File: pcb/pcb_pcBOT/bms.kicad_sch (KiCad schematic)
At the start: 23 parts, among them J201 Lipo, U201 BQ25896RTW

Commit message: manual merge
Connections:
- net SCL_I2C is gone; now on net I2C_SCL: R203.2
- net SDA_I2C is gone; now on net I2C_SDA: R201.2
- net SYS_3.5-4.5V is gone; now on net SYS: C205.1, C207.1, JP202.1 (A), L201.2, U201.15 (SYS), U201.16 (SYS)
- net +5V: now also JP202.2 (B)
- net GND: now also C207.2
- net OTG_HOST: no longer R202.2
- net REGN: now also C204.2
- net STAT: now also R202.2
- net VBUS: now also JP201.1 (A), JP203.1 (A); no longer JP201.2 (B), U201.1 (VBUS)
- net SW: now reaches C203.1, L201.1, U201.19 (SW), U201.20 (SW)
- net BTST: now reaches C203.2, U201.21 (BTST)
- net BAT: now reaches C206.1, J201.1 (Pin_1), U201.13 (BAT), U201.14 (BAT)
- net TS: now reaches R207.2, R208.1, U201.11 (TS)
- net ILIM: now reaches R206.2, U201.10 (ILIM)
- net I2C_SCL: now reaches U201.5 (SCL)
- net PHY: no longer names the net of JP203.2 (B), U201.2 (PSEL)
- net VREF renamed +3.3V
- new net: JP201.2 (B), U201.1 (VBUS)
- no-connect marks 1 -> 0
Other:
- moved on the sheet: R206

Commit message: avancement des schematics
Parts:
- renumbered JP203 to JP202, JP202 to JP203
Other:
- company: ENSEA -> ENSEA G5
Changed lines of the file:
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@@
 		(title "Bms bq25896 (typical application)")
 		(rev "1.0")
-		(company "ENSEA")
+		(company "ENSEA G5")
 	)
 	(junction
@@
 		(dnp no)
 		(fields_autoplaced yes)
-		(property "Reference" "#PWR0204"
+		(property "Reference" "#PWR0206"
 			(at 107.95 77.47 0)
 			(effects
@@
 			(project "pcb_pcBOT"
 				(path "/704e4da3-8ee7-458f-8a0f-3fc97e8dc2a6/d67675e6-7dac-4bc7-9bdf-0364d005735e"
-					(reference "#PWR0204")
+					(reference "#PWR0206")
 					(unit 1)
 				)
@@
 		(on_board yes)
 		(dnp no)
-		(property "Reference" "JP203"
+		(property "Reference" "JP202"
 			(at 119.38 70.104 0)
 			(effects
@@
 			(project "pcb_pcBOT"
 				(path "/704e4da3-8ee7-458f-8a0f-3fc97e8dc2a6/d67675e6-7dac-4bc7-9bdf-0364d005735e"
-					(reference "JP203")
+					(reference "JP202")
 					(unit 1)
 				)
@@
 		(on_board yes)
 		(dnp no)
-		(property "Reference" "#PWR0203"
+		(property "Reference" "#PWR0204"
 			(at 74.93 67.31 0)
 			(effects
@@
 			(project "pcb_pcBOT"
 				(path "/704e4da3-8ee7-458f-8a0f-3fc97e8dc2a6/d67675e6-7dac-4bc7-9bdf-0364d005735e"
-					(reference "#PWR0203")
+					(reference "#PWR0204")
 					(unit 1)
 				)
@@
 		(dnp no)
 		(fields_autoplaced yes)
-		(property "Reference" "JP202"
+		(property "Reference" "JP203"
 			(at 189.23 57.15 0)
 			(effects
@@
 			(project "pcb_pcBOT"
 				(path "/704e4da3-8ee7-458f-8a0f-3fc97e8dc2a6/d67675e6-7dac-4bc7-9bdf-0364d005735e"
-					(reference "JP202")
+					(reference "JP203")
 					(unit 1)
 				)
@@
 		(dnp no)
 		(fields_autoplaced yes)
-		(property "Reference" "#PWR0210"
+		(property "Reference" "#PWR0211"
 			(at 182.88 74.93 0)
 			(effects
@@
 			(project "pcb_pcBOT"
 				(path "/704e4da3-8ee7-458f-8a0f-3fc97e8dc2a6/d67675e6-7dac-4bc7-9bdf-0364d005735e"
-					(reference "#PWR0210")
+					(reference "#PWR0211")
 					(unit 1)
 				)
@@
 		(dnp no)
 		(fields_autoplaced yes)
-		(property "Reference" "#PWR0212"
+		(property "Reference" "#PWR0203"
 			(at 69.85 99.06 0)
 			(effects
@@
 			(project ""
 				(path "/704e4da3-8ee7-458f-8a0f-3fc97e8dc2a6/d67675e6-7dac-4bc7-9bdf-0364d005735e"
-					(reference "#PWR0212")
+					(reference "#PWR0203")
 					(unit 1)
 				)
@@
 		(dnp no)
 		(fields_autoplaced yes)
-		(property "Reference" "#PWR0206"
+		(property "Reference" "#PWR0207"
 			(at 133.35 111.76 0)
 			(effects
@@
 			(project ""
 				(path "/704e4da3-8ee7-458f-8a0f-3fc97e8dc2a6/d67675e6-7dac-4bc7-9bdf-0364d005735e"
-					(reference "#PWR0206")
+					(reference "#PWR0207")
 					(unit 1)
 				)
@@
 		(dnp no)
 		(fields_autoplaced yes)
-		(property "Reference" "#PWR0207"
+		(property "Reference" "#PWR0210"
 			(at 170.18 74.93 0)
 			(effects
@@
 			(project "pcb_pcBOT"
 				(path "/704e4da3-8ee7-458f-8a0f-3fc97e8dc2a6/d67675e6-7dac-4bc7-9bdf-0364d005735e"
-					(reference "#PWR0207")
+					(reference "#PWR0210")
 					(unit 1)
 				)
@@
 		(dnp no)
 		(fields_autoplaced yes)
-		(property "Reference" "#PWR0211"
+		(property "Reference" "#PWR0212"
 			(at 187.96 101.6 0)
 			(effects
@@
 			(project "pcb_pcBOT"
 				(path "/704e4da3-8ee7-458f-8a0f-3fc97e8dc2a6/d67675e6-7dac-4bc7-9bdf-0364d005735e"
-					(reference "#PWR0211")
-					(unit 1)
-				)
+					(reference "#PWR0212")
+					(unit 1)
+				)

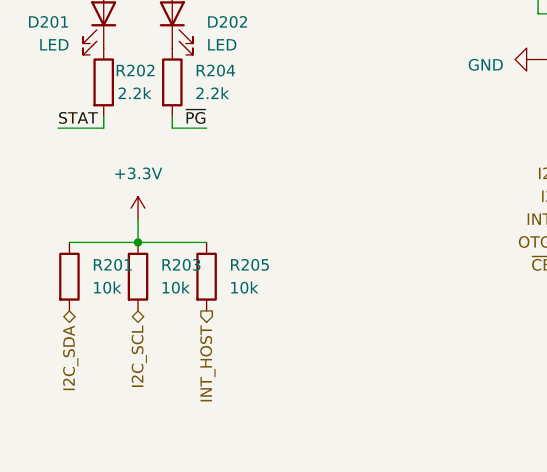
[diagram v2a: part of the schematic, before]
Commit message: ajout du module nrf + petites corrections
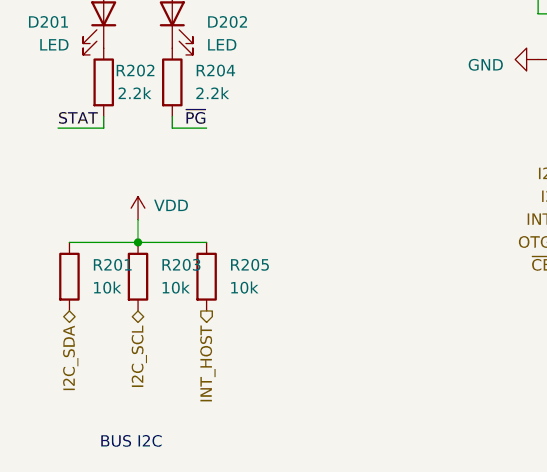
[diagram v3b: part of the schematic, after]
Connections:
- net +3.3V renamed VDD
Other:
- note added: "BUS I2C"
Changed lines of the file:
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@@
 		(company "ENSEA G5")
+	)
+	(text "BUS I2C\n"
+		(exclude_from_sim no)
+		(at 69.088 120.142 0)
+		(effects
+			(font
+				(size 1.27 1.27)
+			)
+		)
 	)
 	(junction
@@
 			)
 			(justify right)
+		)
+	)
+	(rule_area
+		(polyline
+			(pts
+				(xy 50.8 91.44) (xy 88.9 91.44) (xy 88.9 118.11) (xy 50.8 118.11)
+			)
+			(stroke
+				(width 0)
+				(type dash)
+			)
+			(fill
+				(type none)
+			)
 		)
 	)
@@
 		(on_board yes)
 		(dnp no)
-		(fields_autoplaced yes)
 		(property "Reference" "#PWR0203"
 			(at 69.85 99.06 0)
@@
 			)
 		)
-		(property "Value" "+3.3V"
-			(at 69.85 90.17 0)
-			(effects
-				(font
-					(size 1.27 1.27)
-				)
-			)
-		)
+		(property "Value" "VDD"
+			(at 71.628 93.726 0)
+			(effects
+				(font
+					(size 1.27 1.27)
+				)
+				(justify left)
+			)
+		)

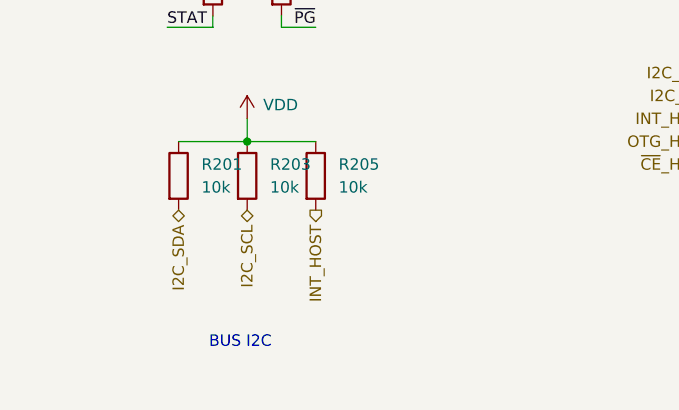
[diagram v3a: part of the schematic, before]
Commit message: complement tof et connections, mise a jour du firmware
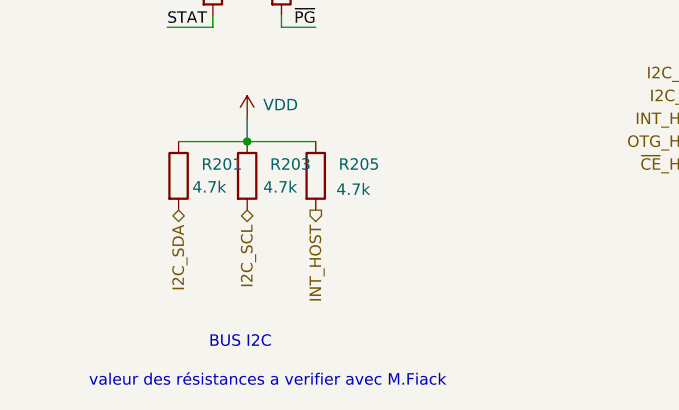
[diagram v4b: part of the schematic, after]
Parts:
- R201, R203, R205: value 10k -> 4.7k
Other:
- note added: "valeur des résistances a verifier avec M.Fiack"
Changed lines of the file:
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@@
+		)
+	)
+	(text "valeur des résistances a verifier avec M.Fiack\n"
+		(exclude_from_sim no)
+		(at 72.136 124.46 0)
+		(effects
+			(font
+				(size 1.27 1.27)
+			)
 		)
 	)
@@
 		(on_board yes)
 		(dnp no)
-		(fields_autoplaced yes)
 		(property "Reference" "R201"
 			(at 64.77 100.3299 0)
@@
 			)
 		)
-		(property "Value" "10k"
-			(at 64.77 102.8699 0)
+		(property "Value" "4.7k"
+			(at 63.754 102.87 0)
 			(effects
 				(font
@@
 		(on_board yes)
 		(dnp no)
-		(fields_autoplaced yes)
 		(property "Reference" "R205"
 			(at 80.01 100.3299 0)
@@
 			)
 		)
-		(property "Value" "10k"
-			(at 80.01 102.8699 0)
+		(property "Value" "4.7k"
+			(at 79.756 103.124 0)
 			(effects
 				(font
@@
 		(on_board yes)
 		(dnp no)
-		(fields_autoplaced yes)
 		(property "Reference" "R203"
 			(at 72.39 100.3299 0)
@@
 			)
 		)
-		(property "Value" "10k"
-			(at 72.39 102.8699 0)
-			(effects
-				(font
+		(property "Value" "4.7k"
+			(at 71.628 102.87 0)
+			(effects
+				(font

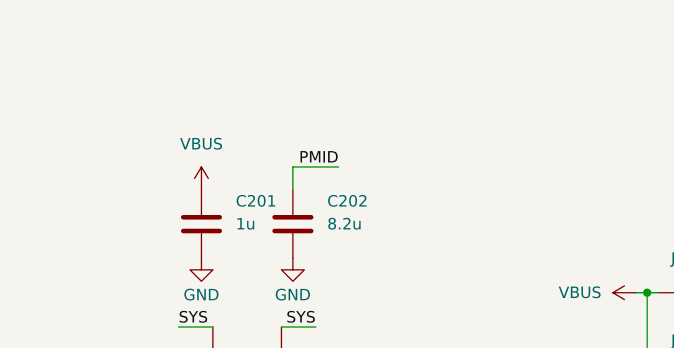
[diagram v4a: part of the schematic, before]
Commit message: corrections d'erreurs et liasons bus i2c et spi
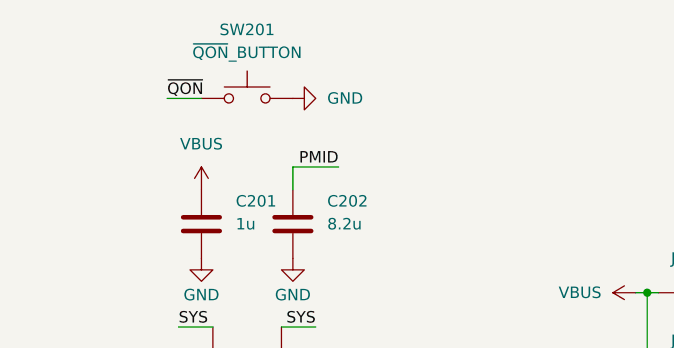
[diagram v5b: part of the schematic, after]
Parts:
- added SW201: ~{QON}_BUTTON, symbol Switch:SW_Push
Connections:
- net GND: now also SW201.2
- new net ~{QON}: SW201.1
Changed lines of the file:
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@@
+	(wire
+		(pts
+			(xy 60.96 43.18) (xy 64.77 43.18)
+		)
+		(stroke
+			(width 0)
+			(type default)
+		)
+	)
 	(wire
 		(pts
@@
 	(label "STAT"
 		(at 118.11 82.55 0)
+		(effects
+			(font
+				(size 1.27 1.27)
+			)
+			(justify left bottom)
+		)
+	)
+	(label "~{QON}"
+		(at 60.96 43.18 0)
 		(effects
 			(font
@@
 	)
 	(symbol
+		(lib_id "Switch:SW_Push")
+		(at 69.85 43.18 0)
+		(unit 1)
+		(exclude_from_sim no)
+		(in_bom yes)
+		(on_board yes)
+		(dnp no)
+		(fields_autoplaced yes)
+		(property "Reference" "SW201"
+			(at 69.85 35.56 0)
+			(effects
+				(font
+					(size 1.27 1.27)
+				)
+			)
+		)
+		(property "Value" "~{QON}_BUTTON"
+			(at 69.85 38.1 0)
+			(effects
+				(font
+					(size 1.27 1.27)
+				)
+			)
+		)
+		(property "Footprint" ""
+			(at 69.85 38.1 0)
+			(effects
+				(font
+					(size 1.27 1.27)
+				)
+				(hide yes)
+			)
+		)
+		(property "Datasheet" "~"
+			(at 69.85 38.1 0)
+			(effects
+				(font
+					(size 1.27 1.27)
+				)
+				(hide yes)
+			)
+		)
+		(property "Description" "Push button switch, generic, two pins"
+			(at 69.85 43.18 0)
+			(effects
+				(font
+					(size 1.27 1.27)
+				)
+				(hide yes)
+			)
+		)
+		(pin "2"
+		)
+		(pin "1"
+		)
+		(instances
+			(project ""
+				(path "/704e4da3-8ee7-458f-8a0f-3fc97e8dc2a6/d67675e6-7dac-4bc7-9bdf-0364d005735e"
+					(reference "SW201")
+					(unit 1)
+				)
+			)
+		)
+	)
+	(symbol
 		(lib_id "power:GND")
 		(at 182.88 68.58 0)
@@
 					(unit 1)
 				)
+			)
+		)
+	)
+	(symbol
+		(lib_id "power:GND")
+		(at 74.93 43.18 90)
+		(unit 1)
+		(exclude_from_sim no)
+		(in_bom yes)
+		(on_board yes)
+		(dnp no)
+		(fields_autoplaced yes)
+		(property "Reference" "#PWR0214"
+			(at 81.28 43.18 0)
+			(effects
+				(font
+					(size 1.27 1.27)
+				)
+				(hide yes)
+			)
+		)
+		(property "Value" "GND"
+			(at 78.74 43.1799 90)
+			(effects
+				(font
+					(size 1.27 1.27)
+				)
+				(justify right)
+			)
+		)
+		(property "Footprint" ""
+			(at 74.93 43.18 0)
+			(effects
+				(font
+					(size 1.27 1.27)
+				)
+				(hide yes)
+			)
+		)
+		(property "Datasheet" ""
+			(at 74.93 43.18 0)
+			(effects
+				(font
+					(size 1.27 1.27)
+				)
+				(hide yes)
+			)
+		)
+		(property "Description" "Power symbol creates a global label with name \"GND\" , ground"
+			(at 74.93 43.18 0)
+			(effects
+				(font
+					(size 1.27 1.27)
+				)
+				(hide yes)
+			)
+		)
+		(pin "1"
+		)
+		(instances
+			(project ""
+				(path "/704e4da3-8ee7-458f-8a0f-3fc97e8dc2a6/d67675e6-7dac-4bc7-9bdf-0364d005735e"
+					(reference "#PWR0214")
+					(unit 1)
+				)

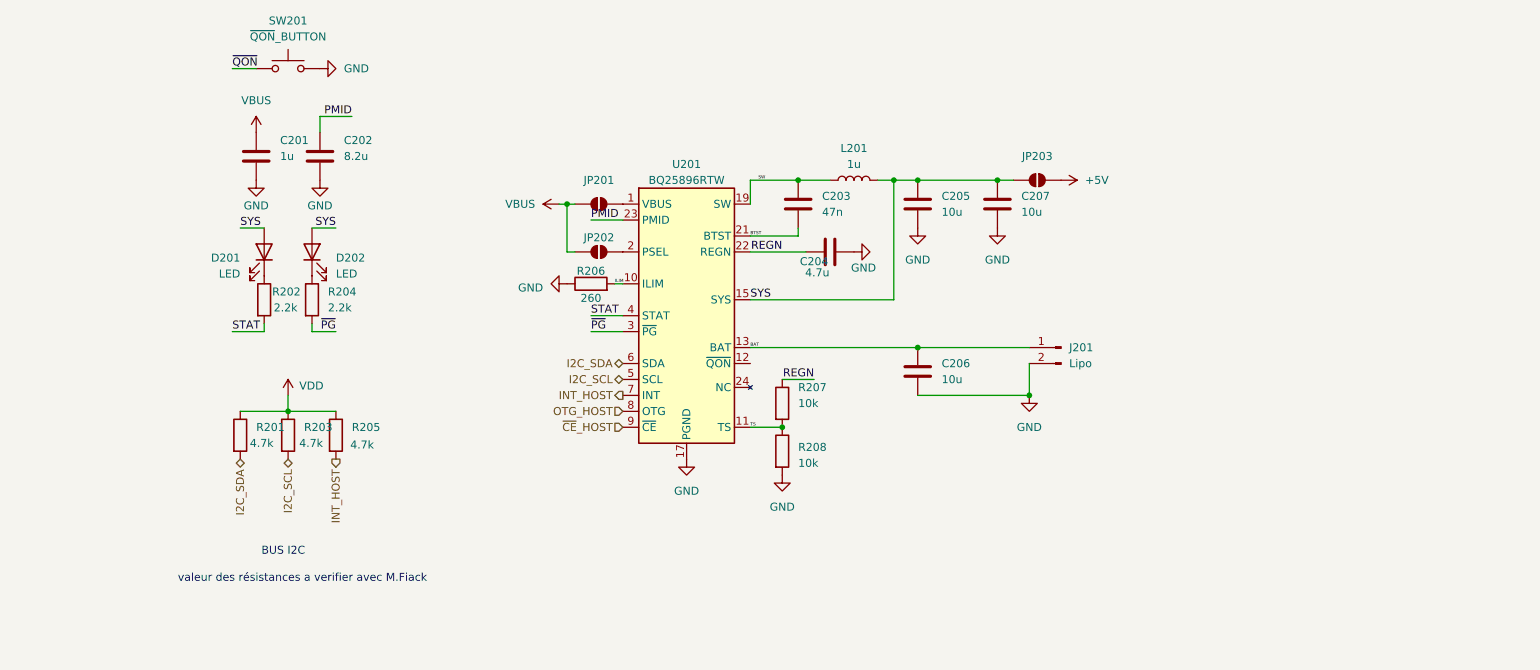
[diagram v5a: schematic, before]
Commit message: Ajout empreintes (incomplet) + test erc correct
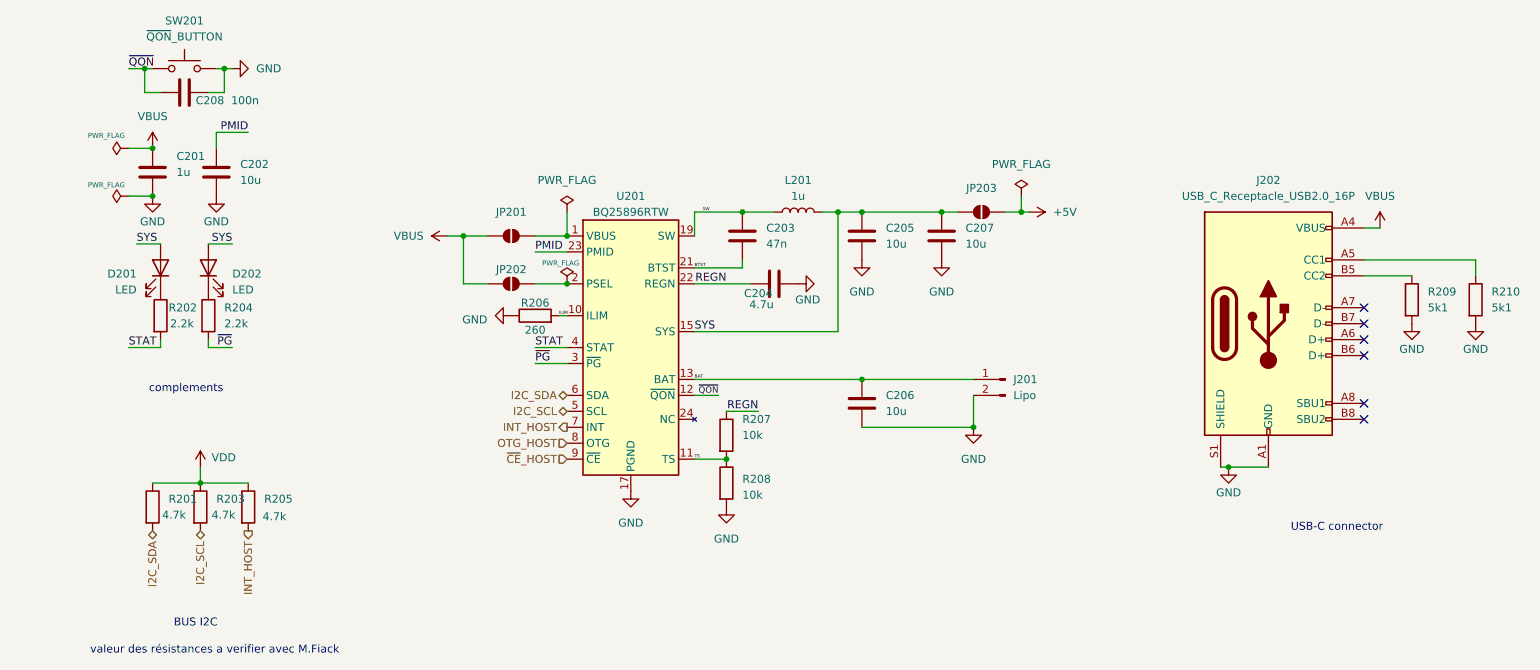
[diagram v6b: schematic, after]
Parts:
- added C208: 100n, Capacitor_SMD:C_0805_2012Metric_Pad1.18x1.45mm_HandSolder, symbol Device:C
- added J202: USB_C_Receptacle_USB2.0_16P, Connector_USB:USB_C_Receptacle_GCT_USB4105-xx-A_16P_TopMnt_Horizontal, symbol Connector:USB_C_Receptacle_USB2.0_16P
- added R209, R210: 5k1, Resistor_SMD:R_0805_2012Metric_Pad1.20x1.40mm_HandSolder, symbol Device:R
- C201, C203, C204, C205, C206, C207: footprint (none) -> Capacitor_SMD:C_0805_2012Metric_Pad1.18x1.45mm_HandSolder
- C202: value 8.2u -> 10u; footprint (none) -> Capacitor_SMD:C_0805_2012Metric_Pad1.18x1.45mm_HandSolder
- D201, D202: footprint (none) -> LED_SMD:LED_0603_1608Metric_Pad1.05x0.95mm_HandSolder
- J201: footprint (none) -> Connector_JST:JST_PH_B2B-PH-K_1x02_P2.00mm_Vertical
- L201: footprint (none) -> Inductor_SMD:L_0805_2012Metric_Pad1.05x1.20mm_HandSolder
- R201, R202, R203, R204, R205, R206, R207, R208: footprint (none) -> Resistor_SMD:R_0805_2012Metric_Pad1.20x1.40mm_HandSolder
- SW201: footprint (none) -> Button_Switch_THT:SW_PUSH_6mm
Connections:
- net GND: now also C208.2, J202.A1 (GND), J202.A12 (GND), J202.B1 (GND), J202.B12 (GND), J202.S1 (SHIELD), R209.2, R210.2
- net VBUS: now also J202.A4 (VBUS), J202.A9 (VBUS), J202.B4 (VBUS), J202.B9 (VBUS)
- net ~{QON}: now also U201.12 (~{QON}), C208.1
- new net: J202.B5 (CC2), R209.1
- new net: J202.A5 (CC1), R210.1
- no-connect marks 0 -> 6
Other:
- note added: "USB-C connector"
- note added: "complements"
- moved on the sheet: C201, C202, C203, C204, C205, C206, C207, D201, D202, J201, JP201, JP202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

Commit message: fin de schematique
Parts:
- removed R201, R203, R205: 4.7k, Resistor_SMD:R_0805_2012Metric_Pad1.20x1.40mm_HandSolder, symbol Device:R
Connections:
- net INT_HOST renamed INT_BMS
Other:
- note added: "BMS BQ25896RTW"
- note removed: "BUS I2C"
- note removed: "valeur des résistances a verifier avec M.Fiack"
- moved on the sheet: C201, C202, C203, C204, C205, C206, C207, C208, D201, D202, J201, J202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

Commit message: schematique terminé + probleme empreinte réglé + début routage
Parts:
- U201: footprint Package_DFN_QFN:Texas_S-PWQFN-N24_EP2.7x2.7mm_ThermalVias -> Package_DFN_QFN:Texas_RTW_WQFN-24-1EP_4x4mm_P0.5mm_EP2.7x2.7mm_ThermalVias
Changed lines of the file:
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@@
 			)
 		)
-		(property "Footprint" "Package_DFN_QFN:Texas_S-PWQFN-N24_EP2.7x2.7mm_ThermalVias"
+		(property "Footprint" "Package_DFN_QFN:Texas_RTW_WQFN-24-1EP_4x4mm_P0.5mm_EP2.7x2.7mm_ThermalVias"
 			(at 116.84 59.69 0)
 			(effects
